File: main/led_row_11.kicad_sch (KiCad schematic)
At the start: 20 parts

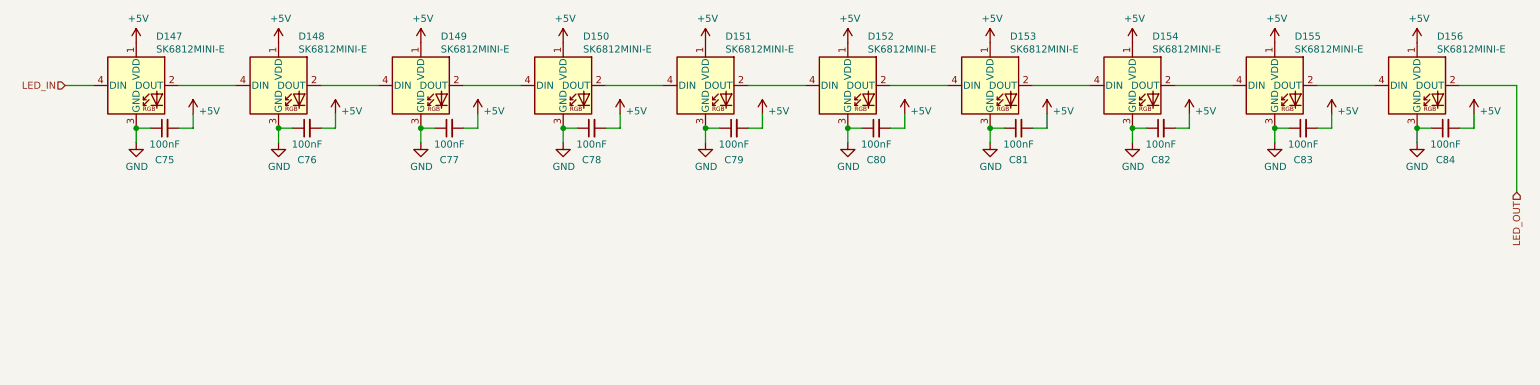
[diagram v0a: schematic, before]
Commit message: Update to new keyboard layout
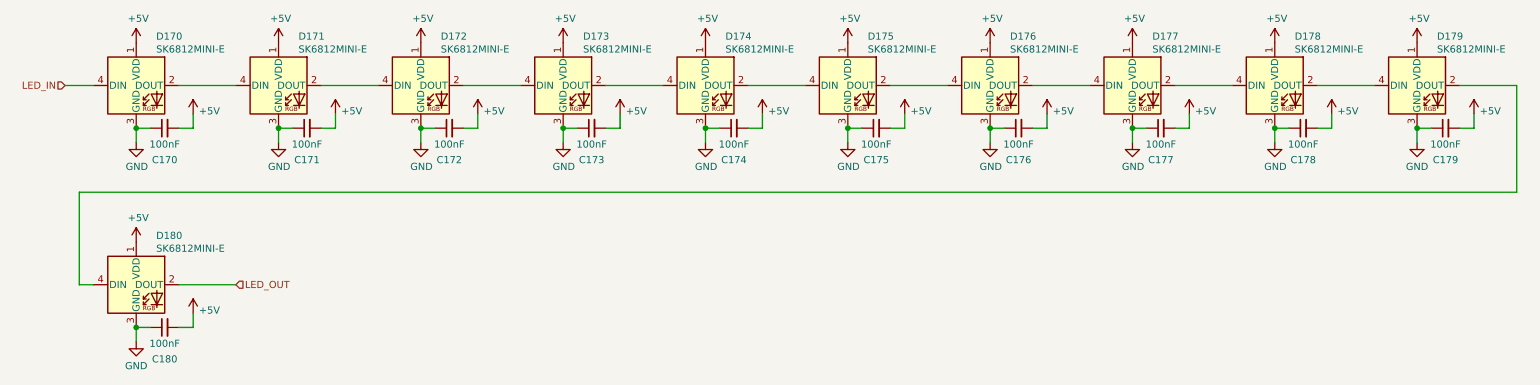
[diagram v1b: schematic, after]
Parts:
- added C180: 100nF, Capacitor_SMD:C_0603_1608Metric, symbol Device:C_Small
- added D180: SK6812MINI-E, chonc60:LED_SK6812_MINI_E_REVERSE, symbol chonc60:SK6812MINI-E
- renumbered C75 to C170, C76 to C171, C77 to C172, C78 to C173, C79 to C174, C80 to C175, C81 to C176, C82 to C177, C83 to C178, C84 to C179, D147 to D170, D148 to D171, D149 to D172, D150 to D173, D151 to D174, D152 to D175, D153 to D176, D154 to D177, D155 to D178, D156 to D179
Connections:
- net +5V: now also C180.2, D180.1 (VDD)
- net GND: now also C180.1, D180.3 (GND)
- net LED_OUT: now also D180.2 (DOUT); no longer D179.2 (DOUT)
- new net: D179.2 (DOUT), D180.4 (DIN)

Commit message: Switch to nRF58420 module and battery power
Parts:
- renumbered C170 to C35, C171 to C36, C172 to C37, C173 to C38, C174 to C39, C175 to C40, C176 to C41, C177 to C42, C178 to C43, C179 to C44, C180 to C45, D170 to D111, D171 to D112, D172 to D113, D173 to D114, D174 to D115, D175 to D116, D176 to D117, D177 to D118, D178 to D119, D179 to D120, D180 to D121
